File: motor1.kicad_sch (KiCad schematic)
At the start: 28 parts, among them J1 Conn_01x01_Pin, J2 Conn_01x01_Pin, J3 Conn_01x01_Pin, Q1 FDMC8010DC, Q2 FDMC8010DC, Q3 FDMC8010DC, Q4 FDMC8010DC, Q5 FDMC8010DC, Q6 FDMC8010DC, U1 GD32E230G8U6, U2 DRV8300D

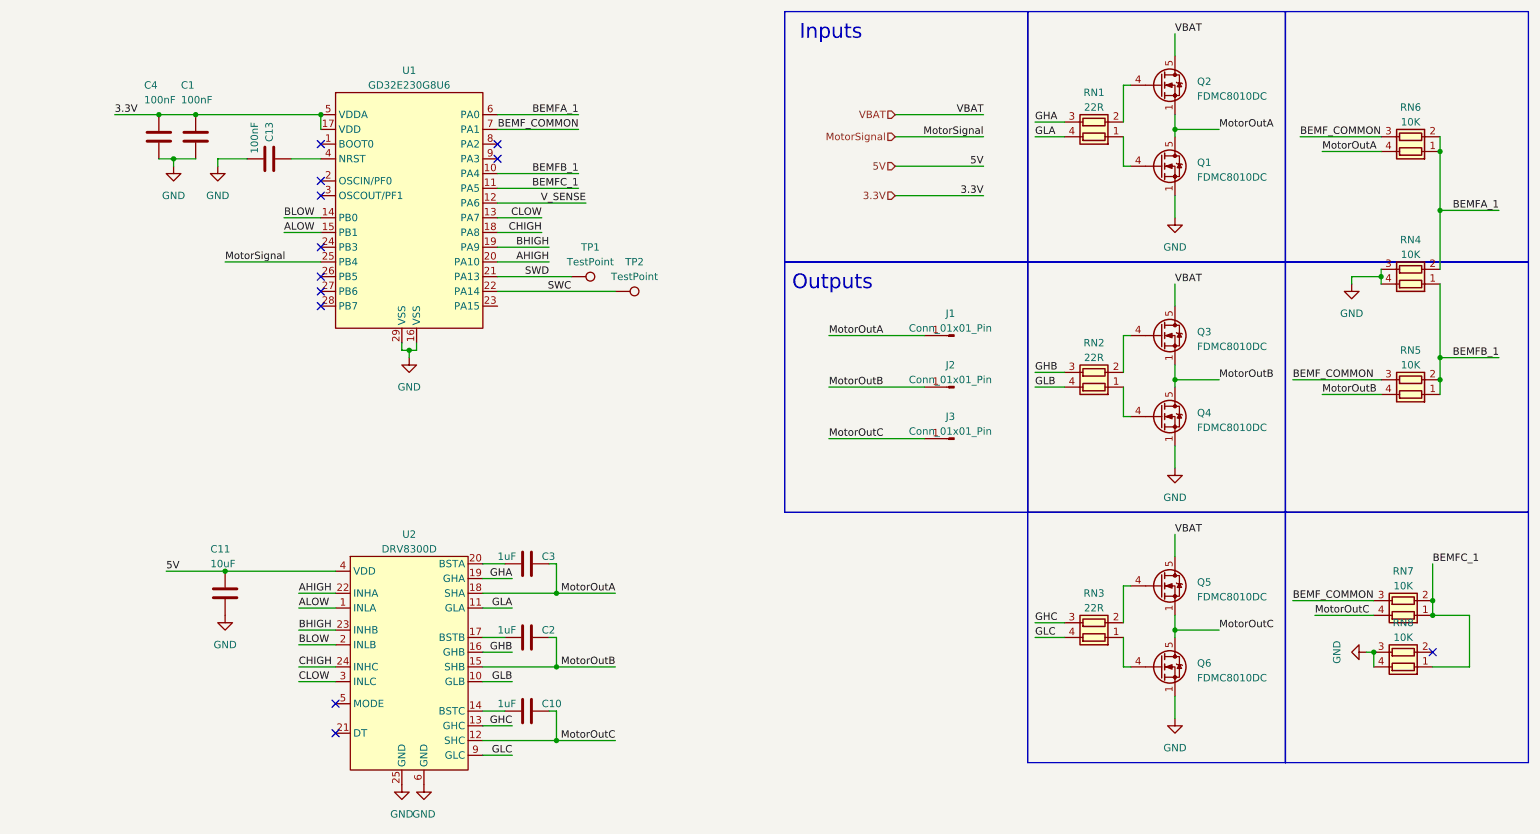
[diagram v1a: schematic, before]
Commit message: Moved top layer fets to allow more current. Other small improvements.
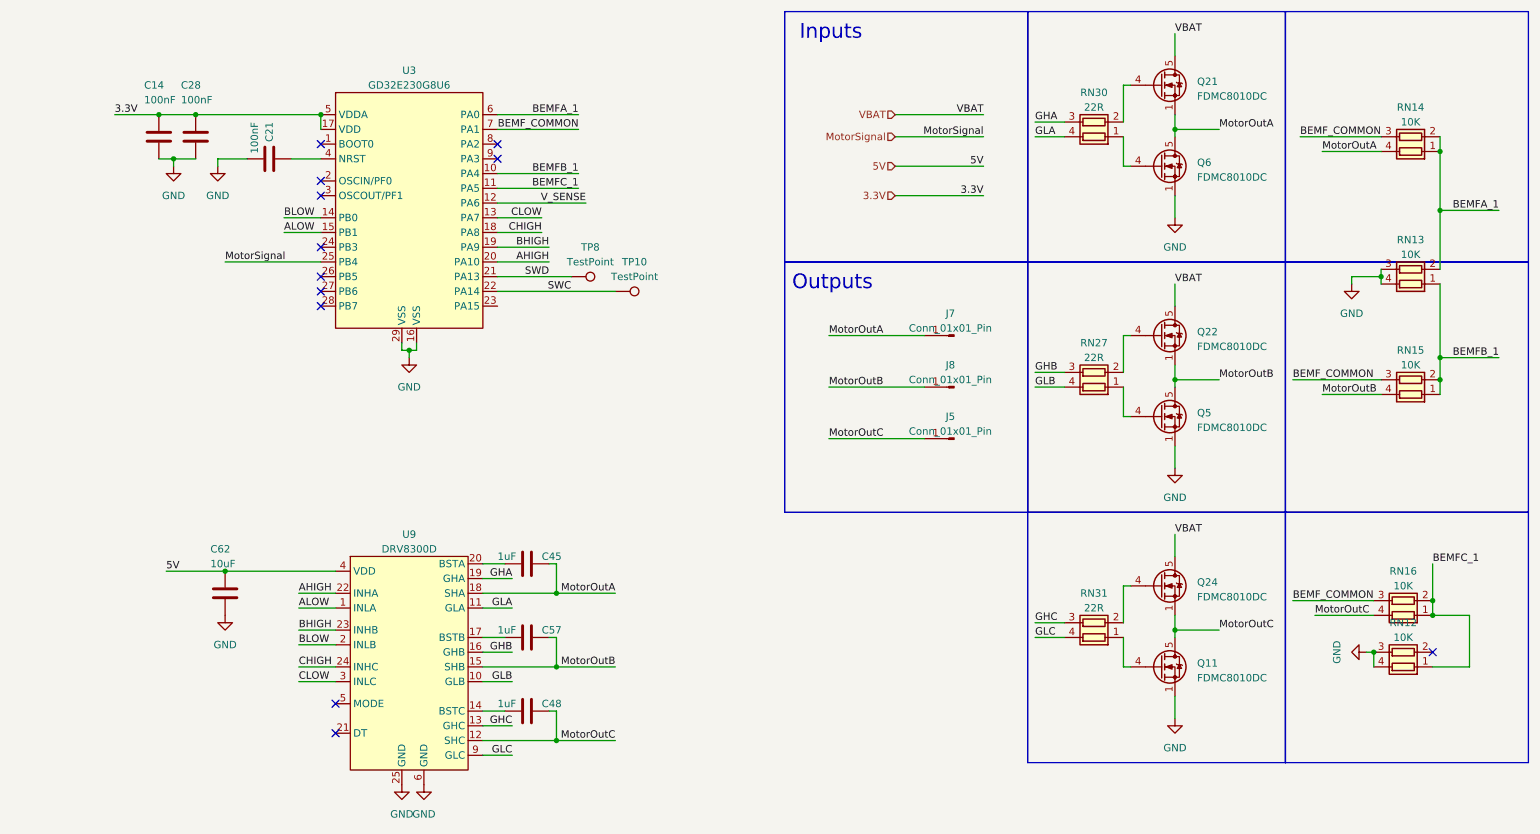
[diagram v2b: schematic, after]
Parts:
- J5: renamed from J3; now left out of the parts list
- J7: renamed from J1; now left out of the parts list
- J8: renamed from J2; now left out of the parts list
- TP10: renamed from TP2; now left out of the parts list
- TP8: renamed from TP1; now left out of the parts list
- renumbered C4 to C14, C13 to C21, C1 to C28, C3 to C45, C10 to C48, C2 to C57, C11 to C62, Q6 to Q11, Q2 to Q21, Q3 to Q22, Q5 to Q24, Q4 to Q5, Q1 to Q6, RN8 to RN12, RN4 to RN13, RN6 to RN14, RN5 to RN15, RN7 to RN16, RN2 to RN27, RN1 to RN30, RN3 to RN31, U1 to U3, U2 to U9

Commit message: Updated power supply scheme. 10V step down to a 3.3V LDO.
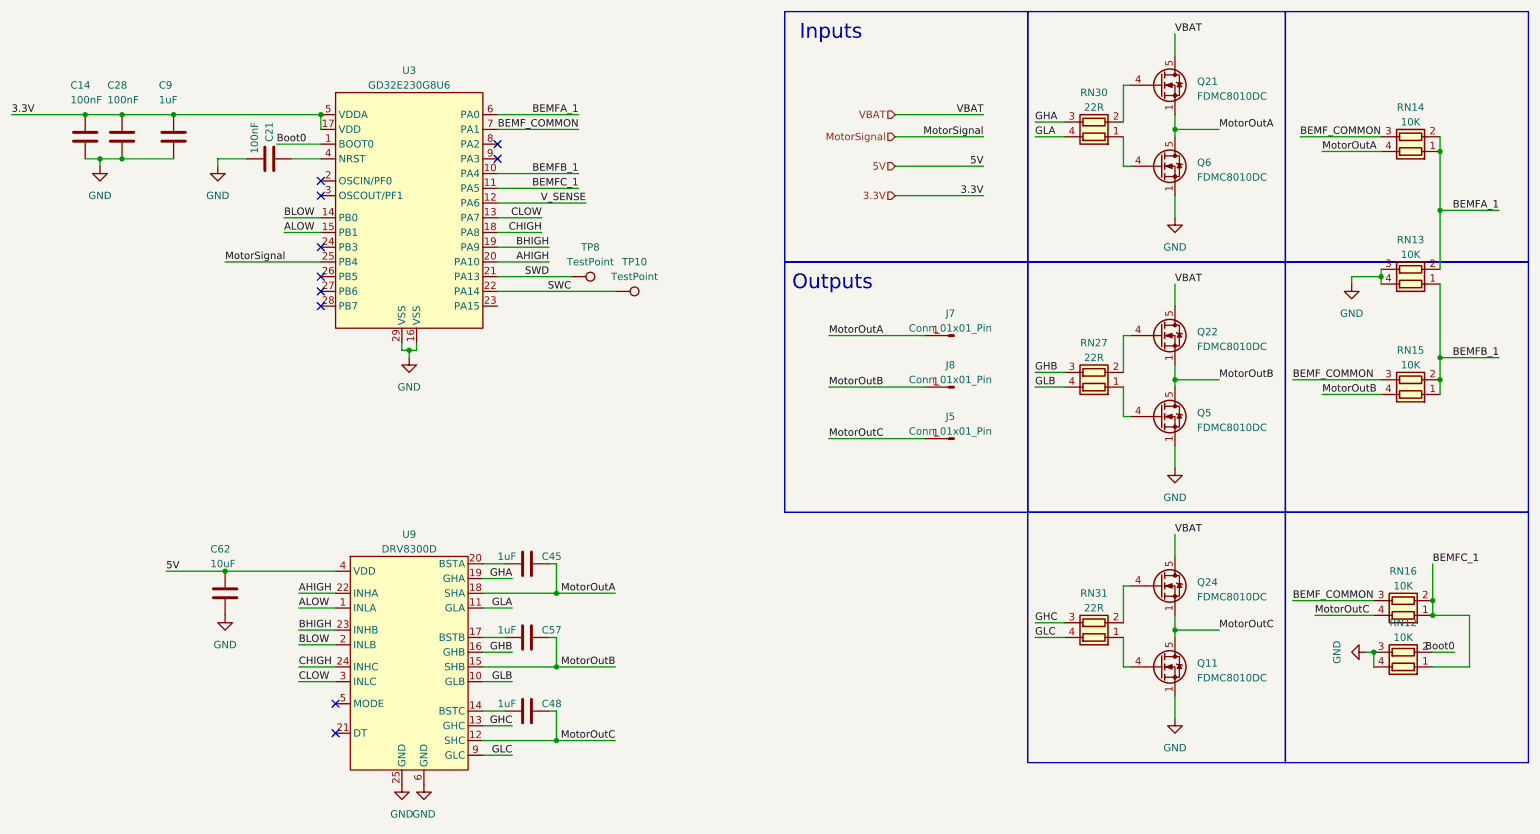
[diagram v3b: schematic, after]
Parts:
- added C9: 1uF, Capacitor_SMD:C_0402_1005Metric, symbol Device:C
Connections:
- net 3.3V: now also C9.1
- net GND: now also C9.2
- net Boot0: now reaches RN12.2 (R2.1)
- net Boot0: now also U3.1 (BOOT0)
- no-connect marks 12 -> 10
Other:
- moved on the sheet: C14, C28
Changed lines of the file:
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@@
   (junction (at 218.44 40.64) (diameter 0) (color 0 0 0 0)
   )
-  (junction (at 43.18 38.1) (diameter 0) (color 0 0 0 0)
+  (junction (at 30.48 38.1) (diameter 0) (color 0 0 0 0)
   )
   (junction (at 262.89 121.92) (diameter 0) (color 0 0 0 0)
@@
   (junction (at 111.76 120.65) (diameter 0) (color 0 0 0 0)
   )
-  (junction (at 49.53 38.1) (diameter 0) (color 0 0 0 0)
+  (junction (at 45.72 38.1) (diameter 0) (color 0 0 0 0)
+  )
+  (junction (at 36.83 38.1) (diameter 0) (color 0 0 0 0)
   )
   (junction (at 254 66.04) (diameter 0) (color 0 0 0 0)
@@
   (junction (at 264.16 54.61) (diameter 0) (color 0 0 0 0)
   )
-  (junction (at 45.72 45.72) (diameter 0) (color 0 0 0 0)
+  (junction (at 33.02 45.72) (diameter 0) (color 0 0 0 0)
   )
   (junction (at 264.16 83.82) (diameter 0) (color 0 0 0 0)
+  )
+  (junction (at 36.83 45.72) (diameter 0) (color 0 0 0 0)
   )
   (junction (at 264.16 44.45) (diameter 0) (color 0 0 0 0)
@@
   (no_connect (at 71.12 49.53))
   (no_connect (at 71.12 60.96))
-  (no_connect (at 262.89 130.81))
   (no_connect (at 71.12 68.58))
   (no_connect (at 71.12 52.07))
   (no_connect (at 101.6 43.18))
-  (no_connect (at 71.12 43.18))
   (no_connect (at 71.12 66.04))
   (no_connect (at 73.66 144.78))
@@
     (stroke (width 0) (type default))
   )
+  (wire (pts (xy 266.7 130.81) (xy 262.89 130.81))
+    (stroke (width 0) (type default))
+  )
   (wire (pts (xy 53.34 45.72) (xy 58.42 45.72))
     (stroke (width 0) (type default))
@@
     (stroke (width 0) (type default))
   )
-  (wire (pts (xy 35.56 38.1) (xy 43.18 38.1))
+  (wire (pts (xy 17.78 38.1) (xy 30.48 38.1))
     (stroke (width 0) (type default))
   )
@@
     (stroke (width 0) (type default))
   )
+  (wire (pts (xy 45.72 38.1) (xy 71.12 38.1))
+    (stroke (width 0) (type default))
+  )
   (wire (pts (xy 218.44 67.31) (xy 218.44 71.12))
     (stroke (width 0) (type default))
@@
     (stroke (width 0) (type default))
   )
-  (wire (pts (xy 43.18 45.72) (xy 45.72 45.72))
+  (wire (pts (xy 30.48 45.72) (xy 33.02 45.72))
     (stroke (width 0) (type default))
   )
@@
     (stroke (width 0) (type default))
   )
+  (wire (pts (xy 36.83 45.72) (xy 45.72 45.72))
+    (stroke (width 0) (type default))
+  )
   (wire (pts (xy 111.76 140.97) (xy 111.76 146.05))
     (stroke (width 0) (type default))
   )
+  (wire (pts (xy 63.5 43.18) (xy 71.12 43.18))
+    (stroke (width 0) (type default))
+  )
   (wire (pts (xy 158.75 93.98) (xy 175.26 93.98))
     (stroke (width 0) (type default))
@@
     (stroke (width 0) (type default))
   )
-  (wire (pts (xy 49.53 38.1) (xy 71.12 38.1))
+  (wire (pts (xy 36.83 38.1) (xy 45.72 38.1))
     (stroke (width 0) (type default))
   )
@@
     (stroke (width 0) (type default))
   )
-  (wire (pts (xy 45.72 46.99) (xy 45.72 45.72))
+  (wire (pts (xy 33.02 46.99) (xy 33.02 45.72))
     (stroke (width 0) (type default))
   )
@@
     (stroke (width 0) (type default))
   )
-  (wire (pts (xy 45.72 45.72) (xy 49.53 45.72))
+  (wire (pts (xy 33.02 45.72) (xy 36.83 45.72))
     (stroke (width 0) (type default))
   )
@@
     (stroke (width 0) (type default))
   )
-  (wire (pts (xy 43.18 38.1) (xy 49.53 38.1))
+  (wire (pts (xy 30.48 38.1) (xy 36.83 38.1))
     (stroke (width 0) (type default))
   )
@@
     (effects (font (size 1.27 1.27)) (justify left bottom))
   )
+  (label "Boot0" (at 63.5 43.18 0) (fields_autoplaced)
+    (effects (font (size 1.27 1.27)) (justify left bottom))
+  )
   (label "ALOW" (at 64.77 58.42 0) (fields_autoplaced)
     (effects (font (size 1.27 1.27)) (justify left bottom))
@@
     (effects (font (size 1.27 1.27)) (justify left bottom))
   )
+  (label "Boot0" (at 266.7 130.81 180) (fields_autoplaced)
+    (effects (font (size 1.27 1.27)) (justify right bottom))
+  )
   (label "MotorSignal" (at 54.61 63.5 0) (fields_autoplaced)
     (effects (font (size 1.27 1.27)) (justify left bottom))
@@
     (effects (font (size 1.27 1.27)) (justify left bottom))
   )
-  (label "3.3V" (at 35.56 38.1 0) (fields_autoplaced)
+  (label "3.3V" (at 17.78 38.1 0) (fields_autoplaced)
     (effects (font (size 1.27 1.27)) (justify left bottom))
   )
@@
     )
   )
-  (symbol (lib_id "Device:C") (at 49.53 41.91 0) (unit 1)
+  (symbol (lib_id "Device:C") (at 36.83 41.91 0) (unit 1)
     (in_bom yes) (on_board yes) (dnp no)
-    (property "Reference" "C28" (at 46.99 33.02 0)
-      (effects (font (size 1.27 1.27)) (justify left))
-    )
-    (property "Value" "100nF" (at 46.99 35.56 0)
-      (effects (font (size 1.27 1.27)) (justify left))
-    )
-    (property "Footprint" "Capacitor_SMD:C_0402_1005Metric" (at 50.4952 45.72 0)
-      (effects (font (size 1.27 1.27)) hide)
-    )
-    (property "Datasheet" "~" (at 49.53 41.91 0)
+    (property "Reference" "C28" (at 34.29 33.02 0)
+      (effects (font (size 1.27 1.27)) (justify left))
+    )
+    (property "Value" "100nF" (at 34.29 35.56 0)
+      (effects (font (size 1.27 1.27)) (justify left))
+    )
+    (property "Footprint" "Capacitor_SMD:C_0402_1005Metric" (at 37.7952 45.72 0)
+      (effects (font (size 1.27 1.27)) hide)
+    )
+    (property "Datasheet" "~" (at 36.83 41.91 0)
       (effects (font (size 1.27 1.27)) hide)
     )
@@
     )
   )
-  (symbol (lib_id "Device:C") (at 43.18 41.91 0) (unit 1)
+  (symbol (lib_id "Device:C") (at 30.48 41.91 0) (unit 1)
     (in_bom yes) (on_board yes) (dnp no)
-    (property "Reference" "C14" (at 40.64 33.02 0)
-      (effects (font (size 1.27 1.27)) (justify left))
-    )
-    (property "Value" "100nF" (at 40.64 35.56 0)
-      (effects (font (size 1.27 1.27)) (justify left))
-    )
-    (property "Footprint" "Capacitor_SMD:C_0402_1005Metric" (at 44.1452 45.72 0)
-      (effects (font (size 1.27 1.27)) hide)
-    )
-    (property "Datasheet" "~" (at 43.18 41.91 0)
+    (property "Reference" "C14" (at 27.94 33.02 0)
+      (effects (font (size 1.27 1.27)) (justify left))
+    )
+    (property "Value" "100nF" (at 27.94 35.56 0)
+      (effects (font (size 1.27 1.27)) (justify left))
+    )
+    (property "Footprint" "Capacitor_SMD:C_0402_1005Metric" (at 31.4452 45.72 0)
+      (effects (font (size 1.27 1.27)) hide)
+    )
+    (property "Datasheet" "~" (at 30.48 41.91 0)
       (effects (font (size 1.27 1.27)) hide)
     )
@@
     )
   )
-  (symbol (lib_id "power:GND") (at 45.72 46.99 0) (unit 1)
-    (in_bom yes) (on_board yes) (dnp no) (fields_autoplaced)
-    (property "Reference" "#PWR017" (at 45.72 53.34 0)
-      (effects (font (size 1.27 1.27)) hide)
-    )
-    (property "Value" "GND" (at 45.72 52.07 0)
-      (effects (font (size 1.27 1.27)))
-    )
-    (property "Footprint" "" (at 45.72 46.99 0)
-      (effects (font (size 1.27 1.27)) hide)
-    )
-    (property "Datasheet" "" (at 45.72 46.99 0)
-      (effects (font (size 1.27 1.27)) hide)
-    )
+  (symbol (lib_id "Device:C") (at 45.72 41.91 0) (unit 1)
+    (in_bom yes) (on_board yes) (dnp no)
+    (property "Reference" "C9" (at 43.18 33.02 0)
+      (effects (font (size 1.27 1.27)) (justify left))
+    )
+    (property "Value" "1uF" (at 43.18 35.56 0)
+      (effects (font (size 1.27 1.27)) (justify left))
+    )
+    (property "Footprint" "Capacitor_SMD:C_0402_1005Metric" (at 46.6852 45.72 0)
+      (effects (font (size 1.27 1.27)) hide)
+    )
+    (property "Datasheet" "~" (at 45.72 41.91 0)
+      (effects (font (size 1.27 1.27)) hide)
+    )
+    (pin "1")
+    (pin "2")
+    (instances
+      (project "fpv_findland_esc"
+        (path "/2cfc6eb1-5e03-4b7e-aaa4-14496495cf61/e7fd4f58-b509-4a30-9f7c-d480524a9f33"
+          (reference "C9") (unit 1)
+        )
+        (path "/2cfc6eb1-5e03-4b7e-aaa4-14496495cf61/8407e2e3-2cad-4225-932f-793823f971f9"
+          (reference "C18") (unit 1)
+        )
+        (path "/2cfc6eb1-5e03-4b7e-aaa4-14496495cf61/690cc11a-fb24-4e15-bdee-480c422a3a9b"
+          (reference "C69") (unit 1)
+        )
+        (path "/2cfc6eb1-5e03-4b7e-aaa4-14496495cf61/01c4b67f-a928-441a-84eb-98d2fa93ea5e"
+          (reference "C70") (unit 1)
+        )
+      )
+    )
+  )
+  (symbol (lib_id "power:GND") (at 33.02 46.99 0) (unit 1)
+    (in_bom yes) (on_board yes) (dnp no) (fields_autoplaced)
+    (property "Reference" "#PWR017" (at 33.02 53.34 0)
+      (effects (font (size 1.27 1.27)) hide)
+    )
+    (property "Value" "GND" (at 33.02 52.07 0)
+      (effects (font (size 1.27 1.27)))
+    )
+    (property "Footprint" "" (at 33.02 46.99 0)
+      (effects (font (size 1.27 1.27)) hide)
+    )
+    (property "Datasheet" "" (at 33.02 46.99 0)
+      (effects (font (size 1.27 1.27)) hide)
+    )
